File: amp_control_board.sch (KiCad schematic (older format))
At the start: 75 parts, among them J1 Conn_01x03_Male, J2 Conn_01x04_Female, J3 Screw_Terminal_01x03, J4 Screw_Terminal_01x02, J5 Conn_01x04_Female, J6 Conn_02x03_Odd_Even, J7 Conn_01x03_Male, M1 Fan_4pin, M2 Fan_4pin, Q1 BSP89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

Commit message: finished floorplan of top layer
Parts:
- removed J3: Screw_Terminal_01x03, TerminalBlock:TerminalBlock_bornier-3_P5.08mm, symbol Connector:Screw_Terminal_01x03
- added J3: Conn_01x03_Male, Connector_PinHeader_2.54mm:PinHeader_1x03_P2.54mm_Vertical, symbol Connector:Conn_01x03_Male
- C1: footprint Capacitor_SMD:C_0805_2012Metric_Pad1.18x1.45mm_HandSolder -> Capacitor_SMD:CP_Elec_10x12.5
- C13, C15, C16, C18: footprint Resistor_SMD:R_0805_2012Metric_Pad1.20x1.40mm_HandSolder -> Resistor_SMD:R_0402_1005Metric_Pad0.72x0.64mm_HandSolder
- C5, C7, C9: footprint Capacitor_SMD:C_0805_2012Metric_Pad1.18x1.45mm_HandSolder -> Capacitor_SMD:CP_Elec_10x10
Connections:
- wire segments 316 -> 319
- no-connect marks 37 -> 34
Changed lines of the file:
@@
 Text GLabel 950  900  0    50   Input ~ 0
 VIN_DC
-$Comp
-L MCU_ST_STM32F1:STM32F103C8Tx U5
-U 1 1 610AD893
-P 13750 5800
-F 0 "U5" H 13700 4211 50  0000 C CNN
-F 1 "STM32F103C8Tx" H 13700 4120 50  0000 C CNN
-F 2 "Package_QFP:LQFP-48_7x7mm_P0.5mm" H 13150 4400 50  0001 R CNN
-F 3 "http://www.st.com/st-web-ui/static/active/en/resource/technical/document/datasheet/CD00161566.pdf" H 13750 5800 50  0001 C CNN
-	1    13750 5800
-	1    0    0    -1
-$EndComp
 Wire Wire Line
 	13550 7300 13550 7600
@@
 F 0 "C16" H 14465 8646 50  0000 L CNN
 F 1 "100n" H 14465 8555 50  0000 L CNN
-F 2 "Resistor_SMD:R_0805_2012Metric_Pad1.20x1.40mm_HandSolder" H 14388 8450 50  0001 C CNN
+F 2 "Resistor_SMD:R_0402_1005Metric_Pad0.72x0.64mm_HandSolder" H 14388 8450 50  0001 C CNN
 F 3 "~" H 14350 8600 50  0001 C CNN
 	1    14350 8600
@@
 F 0 "C18" H 15265 8646 50  0000 L CNN
 F 1 "100n" H 15265 8555 50  0000 L CNN
-F 2 "Resistor_SMD:R_0805_2012Metric_Pad1.20x1.40mm_HandSolder" H 15188 8450 50  0001 C CNN
+F 2 "Resistor_SMD:R_0402_1005Metric_Pad0.72x0.64mm_HandSolder" H 15188 8450 50  0001 C CNN
 F 3 "~" H 15150 8600 50  0001 C CNN
 	1    15150 8600
@@
 F 0 "C13" H 12815 8646 50  0000 L CNN
 F 1 "100n" H 12815 8555 50  0000 L CNN
-F 2 "Resistor_SMD:R_0805_2012Metric_Pad1.20x1.40mm_HandSolder" H 12738 8450 50  0001 C CNN
+F 2 "Resistor_SMD:R_0402_1005Metric_Pad0.72x0.64mm_HandSolder" H 12738 8450 50  0001 C CNN
 F 3 "~" H 12700 8600 50  0001 C CNN
 	1    12700 8600
@@
 F 0 "C15" H 13665 8646 50  0000 L CNN
 F 1 "100n" H 13665 8555 50  0000 L CNN
-F 2 "Resistor_SMD:R_0805_2012Metric_Pad1.20x1.40mm_HandSolder" H 13588 8450 50  0001 C CNN
+F 2 "Resistor_SMD:R_0402_1005Metric_Pad0.72x0.64mm_HandSolder" H 13588 8450 50  0001 C CNN
 F 3 "~" H 13550 8600 50  0001 C CNN
 	1    13550 8600
@@
 F 0 "C9" H 3865 2496 50  0000 L CNN
 F 1 "10u" H 3865 2405 50  0000 L CNN
-F 2 "Capacitor_SMD:C_0805_2012Metric_Pad1.18x1.45mm_HandSolder" H 3750 2450 50  0001 C CNN
+F 2 "Capacitor_SMD:CP_Elec_10x10" H 3750 2450 50  0001 C CNN
 F 3 "~" H 3750 2450 50  0001 C CNN
 	1    3750 2450
@@
 	-1   0    0    1
 $EndComp
-$Comp
-L Connector:Screw_Terminal_01x03 J3
-U 1 1 61352A05
-P 6200 7850
-F 0 "J3" H 6280 7892 50  0000 L CNN
-F 1 "Screw_Terminal_01x03" H 6280 7801 50  0000 L CNN
-F 2 "TerminalBlock:TerminalBlock_bornier-3_P5.08mm" H 6200 7850 50  0001 C CNN
-F 3 "~" H 6200 7850 50  0001 C CNN
-	1    6200 7850
-	-1   0    0    1
-$EndComp
 Wire Wire Line
 	8750 7800 9000 7800
@@
 NoConn ~ 13050 5200
 NoConn ~ 13050 5700
-NoConn ~ 13050 5900
-NoConn ~ 13050 6000
-NoConn ~ 13050 6100
 NoConn ~ 13050 6500
 NoConn ~ 13050 6600
@@
 F 0 "C1" H 1215 1246 50  0000 L CNN
 F 1 "1u" H 1215 1155 50  0000 L CNN
-F 2 "Capacitor_SMD:C_0805_2012Metric_Pad1.18x1.45mm_HandSolder" H 1138 1050 50  0001 C CNN
+F 2 "Capacitor_SMD:CP_Elec_10x12.5" H 1138 1050 50  0001 C CNN
 F 3 "~" H 1100 1200 50  0001 C CNN
 	1    1100 1200
@@
 F 0 "C7" H 2715 2496 50  0000 L CNN
 F 1 "220n" H 2715 2405 50  0000 L CNN
-F 2 "Capacitor_SMD:C_0805_2012Metric_Pad1.18x1.45mm_HandSolder" H 2638 2300 50  0001 C CNN
+F 2 "Capacitor_SMD:CP_Elec_10x10" H 2638 2300 50  0001 C CNN
 F 3 "~" H 2600 2450 50  0001 C CNN
 	1    2600 2450
@@
 F 0 "C5" H 2415 1246 50  0000 L CNN
 F 1 "220n" H 2415 1155 50  0000 L CNN
-F 2 "Capacitor_SMD:C_0805_2012Metric_Pad1.18x1.45mm_HandSolder" H 2338 1050 50  0001 C CNN
+F 2 "Capacitor_SMD:CP_Elec_10x10" H 2338 1050 50  0001 C CNN
 F 3 "~" H 2300 1200 50  0001 C CNN
 	1    2300 1200
@@
 Text GLabel 4400 8850 1    50   Input ~ 0
 VDD_3V3
+$Comp
+L MCU_ST_STM32F1:STM32F103C8Tx U5
+U 1 1 610AD893
+P 13750 5800
+F 0 "U5" H 13700 4211 50  0000 C CNN
+F 1 "STM32F103C8Tx" H 13700 4120 50  0000 C CNN
+F 2 "Package_QFP:LQFP-48_7x7mm_P0.5mm" H 13150 4400 50  0001 R CNN
+F 3 "http://www.st.com/st-web-ui/static/active/en/resource/technical/document/datasheet/CD00161566.pdf" H 13750 5800 50  0001 C CNN
+	1    13750 5800
+	1    0    0    -1
+$EndComp
+Wire Wire Line
+	13050 5900 12550 5900
+Wire Wire Line
+	13050 6000 12550 6000
+Wire Wire Line
+	13050 6100 12550 6100
+Text GLabel 12550 5900 0    50   Input ~ 0
+BTN_MODE
+Text GLabel 12550 6000 0    50   Input ~ 0
+BTN_UP
+Text GLabel 12550 6100 0    50   Input ~ 0
+BTN_DOWN
+$Comp
+L Connector:Conn_01x03_Male J3
+U 1 1 6131EF38
+P 6200 7850
+F 0 "J3" H 6308 8131 50  0000 C CNN
+F 1 "Conn_01x03_Male" H 6308 8040 50  0000 C CNN
+F 2 "Connector_PinHeader_2.54mm:PinHeader_1x03_P2.54mm_Vertical" H 6200 7850 50  0001 C CNN
+F 3 "~" H 6200 7850 50  0001 C CNN
+	1    6200 7850
+	1    0    0    1
+$EndComp
 $EndSCHEMATC

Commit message: completed preliminary floorplan for both top and bottom
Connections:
- no-connect marks 34 -> 35
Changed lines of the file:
@@
 	1    0    0    1
 $EndComp
+NoConn ~ 1800 1000
 $EndSCHEMATC

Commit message: top routing about 70% done
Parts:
- added H1, H2, H3, H4: MountingHole, MountingHole:MountingHole_2.5mm_Pad, symbol Mechanical:MountingHole
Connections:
- net BTN_DOWN: now also U5.39 (PB3); no longer U5.41 (PB5)
- net BTN_MODE: now also U5.41 (PB5); no longer U5.39 (PB3)
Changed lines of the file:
@@
 $EndComp
 Wire Wire Line
-	13050 5900 12550 5900
+	13050 6100 12550 6100
 Wire Wire Line
 	13050 6000 12550 6000
 Wire Wire Line
-	13050 6100 12550 6100
-Text GLabel 12550 5900 0    50   Input ~ 0
+	13050 5900 12550 5900
+Text GLabel 12550 6100 0    50   Input ~ 0
 BTN_MODE
 Text GLabel 12550 6000 0    50   Input ~ 0
 BTN_UP
-Text GLabel 12550 6100 0    50   Input ~ 0
+Text GLabel 12550 5900 0    50   Input ~ 0
 BTN_DOWN
 $Comp
@@
 $EndComp
 NoConn ~ 1800 1000
+$Comp
+L Mechanical:MountingHole H1
+U 1 1 61241D96
+P 1000 6850
+F 0 "H1" H 1100 6896 50  0000 L CNN
+F 1 "MountingHole" H 1100 6805 50  0000 L CNN
+F 2 "MountingHole:MountingHole_2.5mm_Pad" H 1000 6850 50  0001 C CNN
+F 3 "~" H 1000 6850 50  0001 C CNN
+	1    1000 6850
+	1    0    0    -1
+$EndComp
+$Comp
+L Mechanical:MountingHole H2
+U 1 1 612435FE
+P 1750 6850
+F 0 "H2" H 1850 6896 50  0000 L CNN
+F 1 "MountingHole" H 1850 6805 50  0000 L CNN
+F 2 "MountingHole:MountingHole_2.5mm_Pad" H 1750 6850 50  0001 C CNN
+F 3 "~" H 1750 6850 50  0001 C CNN
+	1    1750 6850
+	1    0    0    -1
+$EndComp
+$Comp
+L Mechanical:MountingHole H3
+U 1 1 612444F6
+P 2500 6850
+F 0 "H3" H 2600 6896 50  0000 L CNN
+F 1 "MountingHole" H 2600 6805 50  0000 L CNN
+F 2 "MountingHole:MountingHole_2.5mm_Pad" H 2500 6850 50  0001 C CNN
+F 3 "~" H 2500 6850 50  0001 C CNN
+	1    2500 6850
+	1    0    0    -1
+$EndComp
+$Comp
+L Mechanical:MountingHole H4
+U 1 1 612453FE
+P 3250 6850
+F 0 "H4" H 3350 6896 50  0000 L CNN
+F 1 "MountingHole" H 3350 6805 50  0000 L CNN
+F 2 "MountingHole:MountingHole_2.5mm_Pad" H 3250 6850 50  0001 C CNN
+F 3 "~" H 3250 6850 50  0001 C CNN
+	1    3250 6850
+	1    0    0    -1
+$EndComp
 $EndSCHEMATC

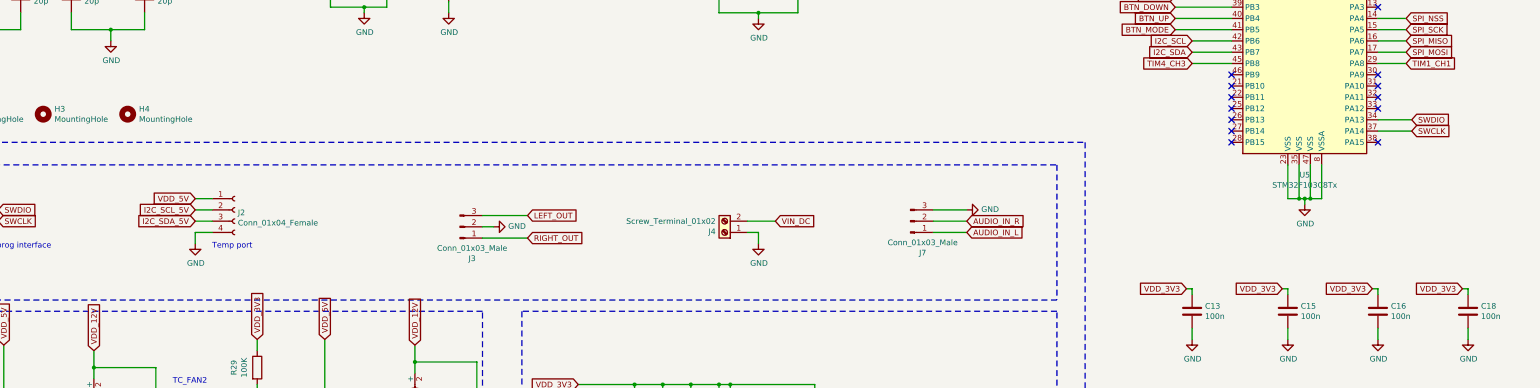
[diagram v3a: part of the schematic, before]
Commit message: routed some more on top layer, added USB interface
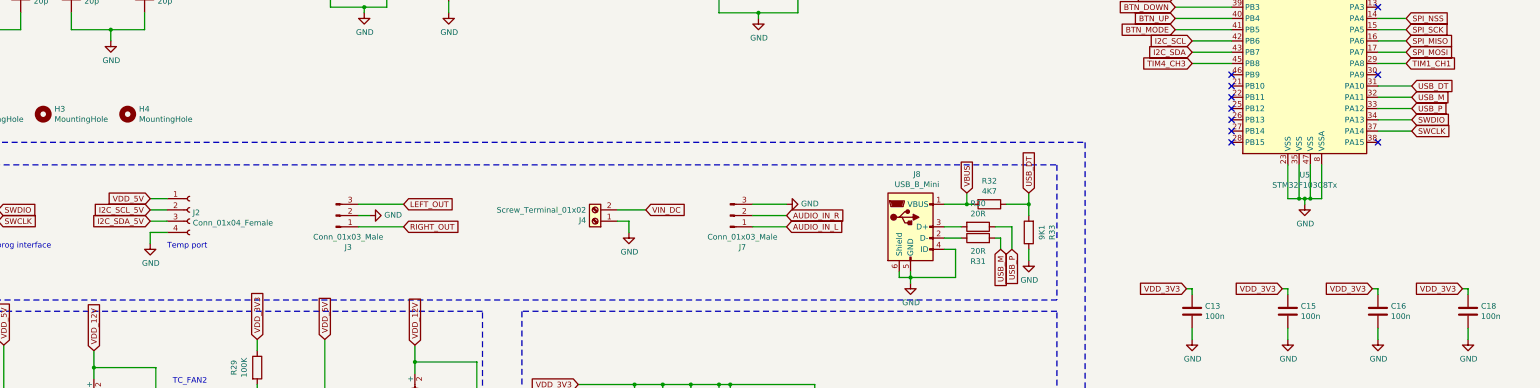
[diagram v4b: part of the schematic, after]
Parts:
- added J8: USB_B_Mini, Connector_USB:USB_Mini-B_Lumberg_2486_01_Horizontal, symbol Connector:USB_B_Mini
- added R30, R31: 20R, Resistor_SMD:R_0402_1005Metric_Pad0.72x0.64mm_HandSolder, symbol Device:R
- added R32: 4K7, Resistor_SMD:R_0805_2012Metric_Pad1.20x1.40mm_HandSolder, symbol Device:R
- added R33: 9K1, Resistor_SMD:R_0805_2012Metric_Pad1.20x1.40mm_HandSolder, symbol Device:R
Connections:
- net GND: now also J8.4 (ID), J8.5 (GND), J8.6 (Shield), R33.1
- net USB_DT: now reaches U5.31 (PA10)
- net USB_DT: now also R32.1, R33.2
- net USB_M: now reaches U5.32 (PA11)
- net USB_M: now also R31.2
- net USB_P: now reaches U5.33 (PA12)
- net USB_P: now also R30.1
- new net: J8.2 (D-), R31.1
- new net: J8.3 (D+), R30.2
- new net VBUS: J8.1 (VBUS), R32.2
- no-connect marks 35 -> 32
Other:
- moved on the sheet: J2, J3, J4, J7

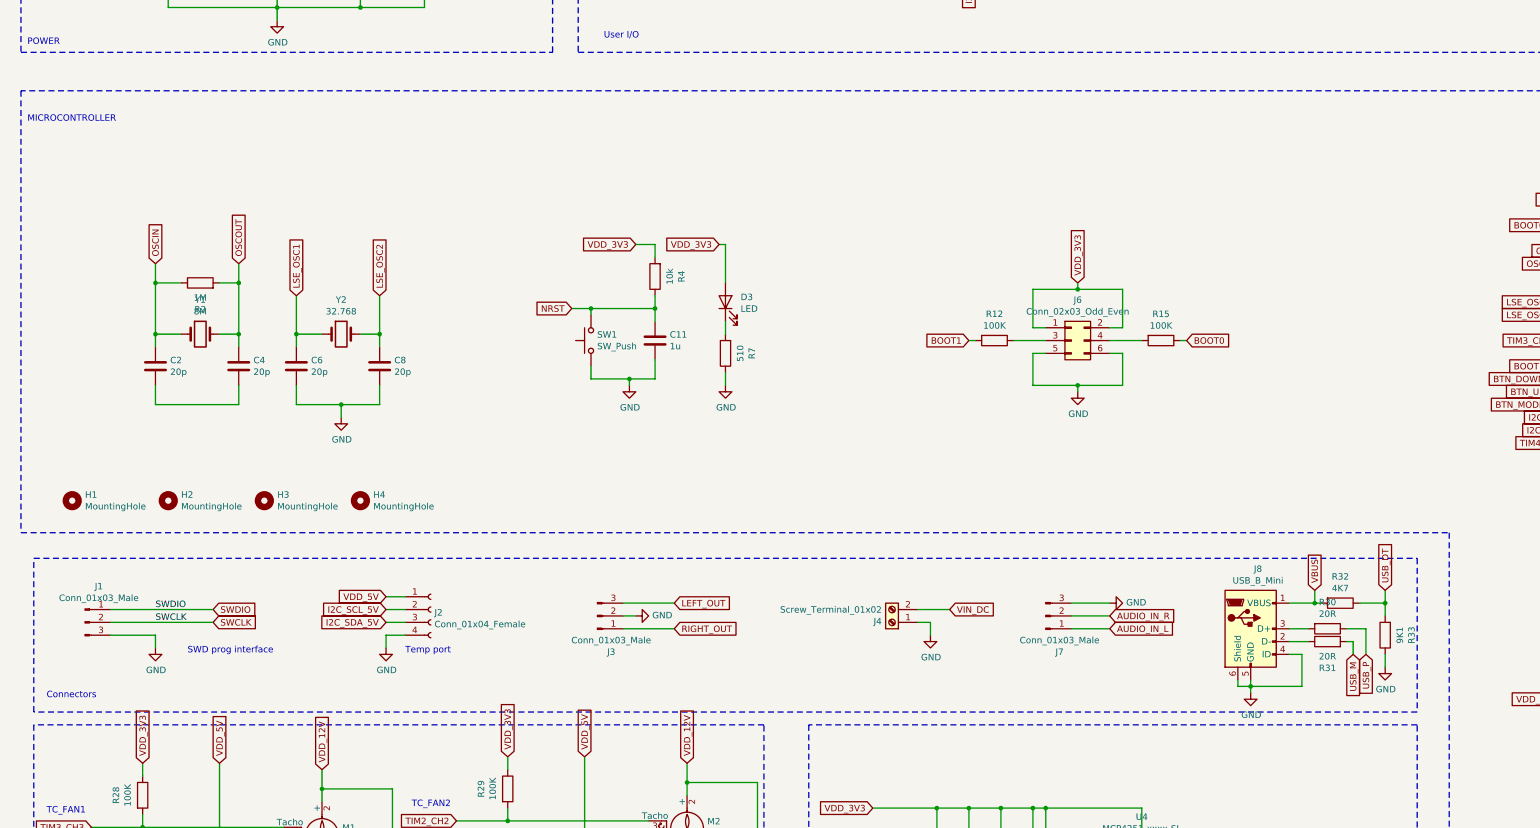
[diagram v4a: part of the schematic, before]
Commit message: added USB protection
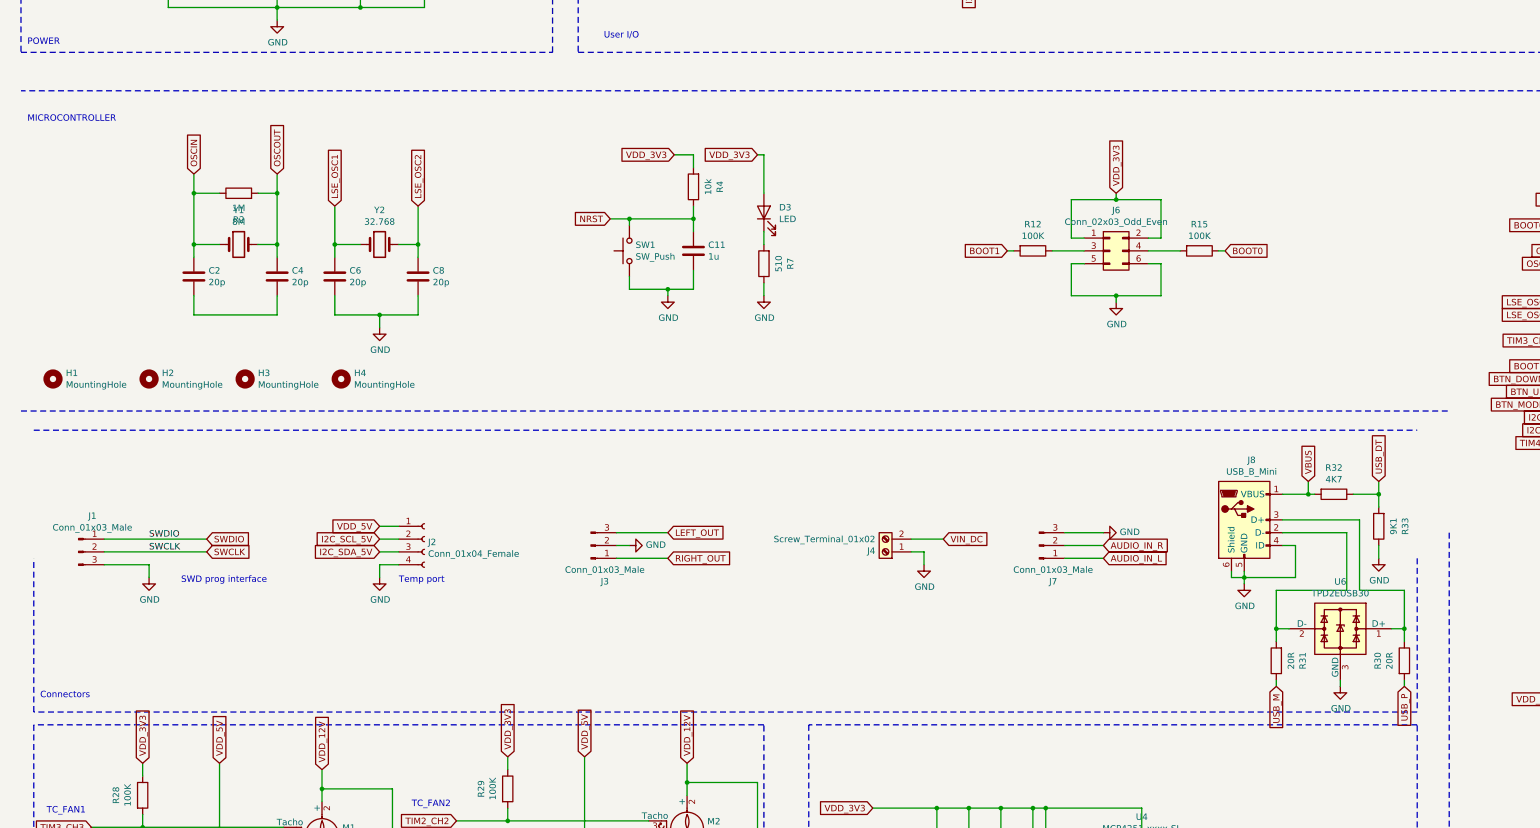
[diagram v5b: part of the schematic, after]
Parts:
- added U6: TPD2EUSB30, Package_TO_SOT_SMD:Texas_DRT-3, symbol Power_Protection:TPD2EUSB30
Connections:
- net GND: now also U6.3 (GND)
- net USB_M: now also R31.1; no longer R31.2
- net USB_P: now also R30.2; no longer R30.1
- net at J8.2 (D-): now also R31.2, U6.2 (D-); no longer R31.1
- net at J8.3 (D+): now also R30.1, U6.1 (D+); no longer R30.2
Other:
- moved on the sheet: C11, C2, C4, C6, C8, D3, H1, H2, H3, H4, J1, J2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
